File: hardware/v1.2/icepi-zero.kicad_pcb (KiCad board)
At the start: 4 copper layers, 65 x 30 mm, 160 parts, among them J1 Conn_02x20_Counter_Clockwise, J2 HDMI_C_1.3, J3 USB_C_Receptacle_USB2.0_14P, J4 USB_C_Receptacle_USB2.0_14P, J5 USB_C_Receptacle_USB2.0_14P, J6 Micro_SD_Card_Det2, SW1 SW_Push, SW2 SW_Push, U1 ECP5-CABGA256, U10 W9825G6KH, U11 W25Q128JVS, U2 TLV62569DBV, U3 TLV62569DBV, U4 TLV62569DBV, U5 PCA9306DC1, U6 FT231XQ, U7 TPD2EUSB30A, U8 TPD2EUSB30A, U9 TPD2EUSB30A, Y1 SITxxxxxx-1x-33E-50.000000

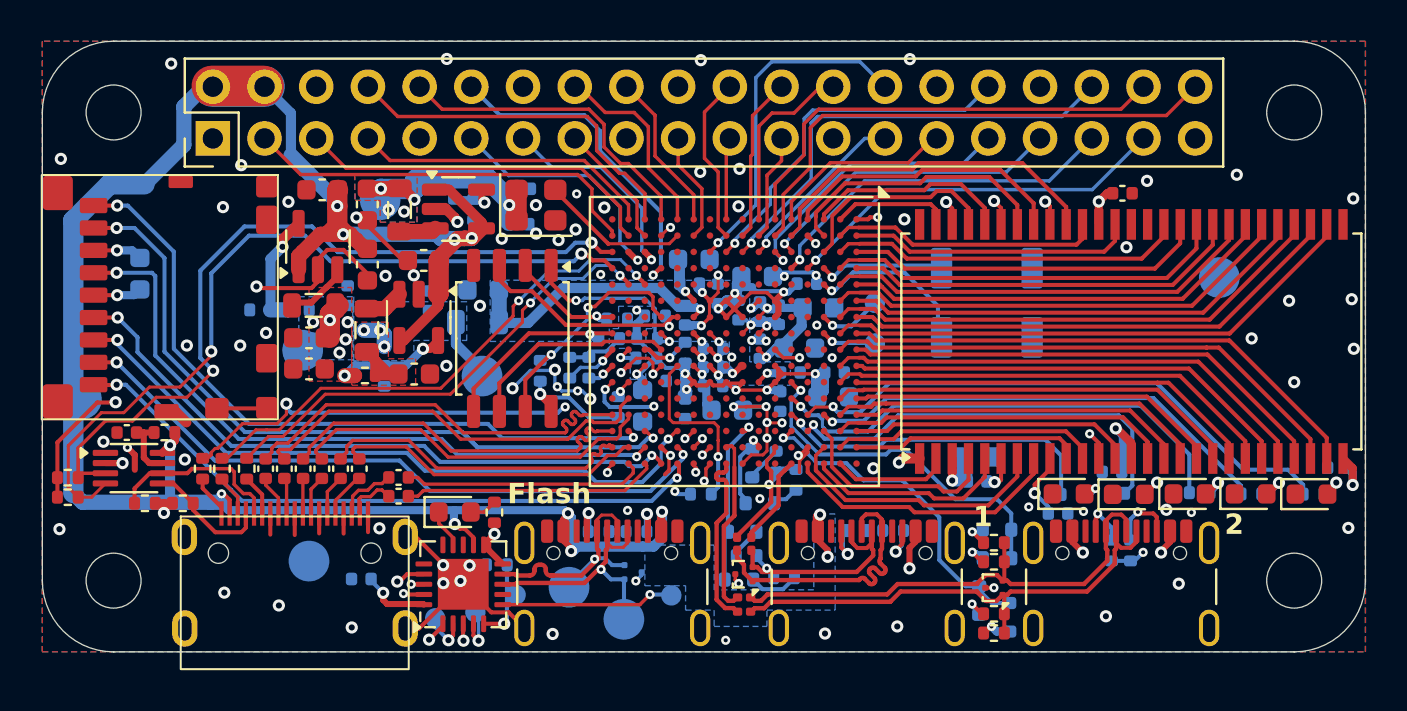
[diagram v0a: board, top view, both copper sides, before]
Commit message: UART to PS2 converter
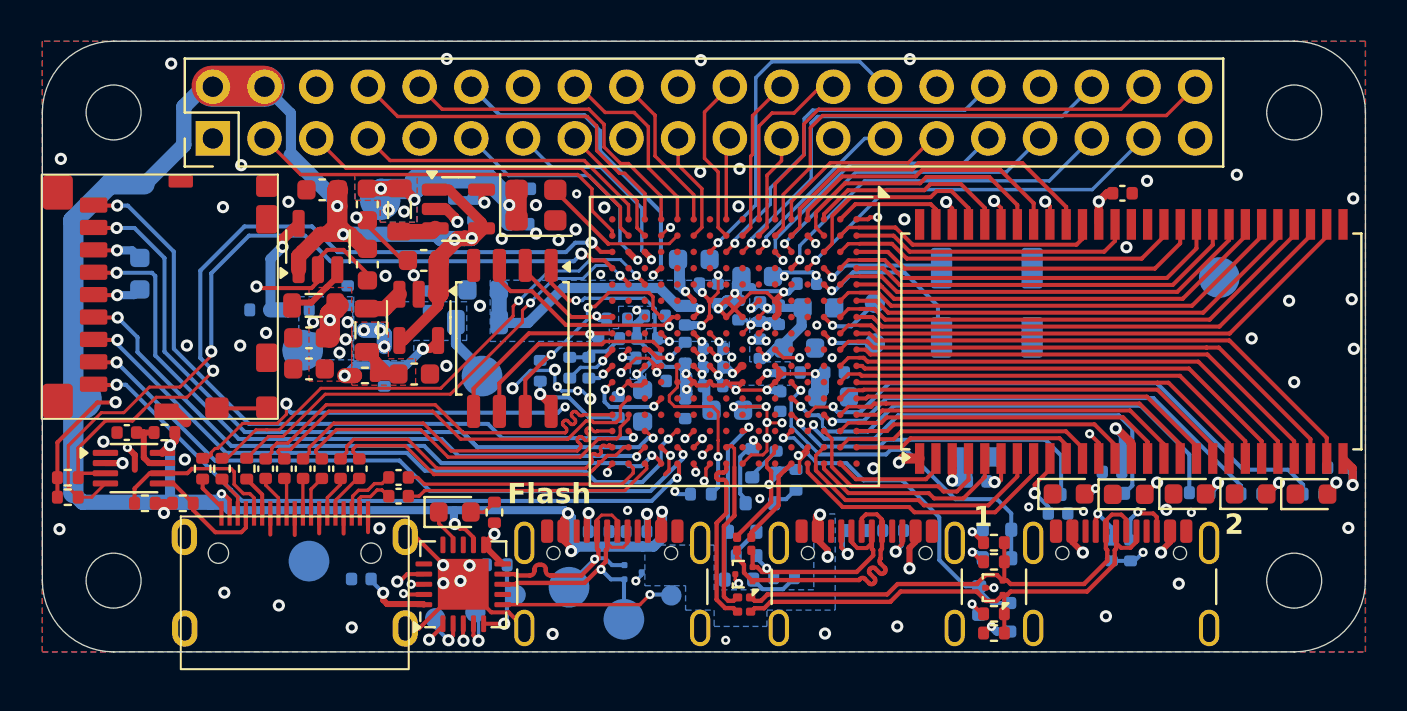
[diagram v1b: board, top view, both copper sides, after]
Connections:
- U1 pad M11: unconnected-(U1J-PR47A/+/HS/RSQ44-PadM11) -> JTAG_TDO
- U1 pad M9: unconnected-(U1J-PB18A/WRITEN-PadM9) -> (no net)
- U1 pad N12: unconnected-(U1J-PR44D/-/RSQ44-PadN12) -> JTAG_TMS
- U1 pad P11: unconnected-(U1J-PR47C/+/RSQ44/LRC_GPLL0T_IN-PadP11) -> JTAG_TDI
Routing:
- net JTAG_TDI: track 31.7 -> 32.6 mm
- net +3V3: track 95.4 -> 96.1 mm
- net JTAG_TMS: track 34.0 -> 34.5 mm

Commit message: Improve Makefile and v1.0 lpf
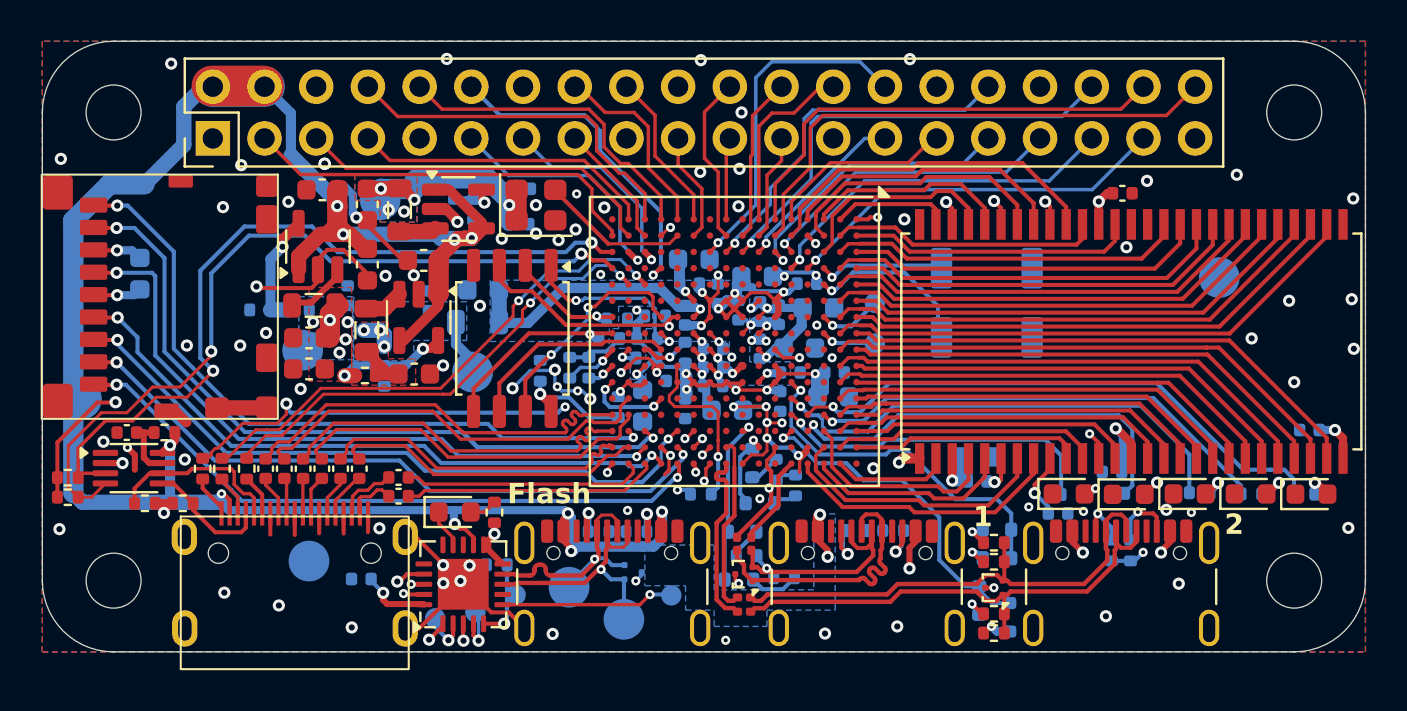
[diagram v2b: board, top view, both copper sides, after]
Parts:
- Y1: value SITxxxxxx-1x-33E-50.000000 -> SG-8018CG 50.000000MHz
- moved C39 2.31 mm to (178.2, 109.1)
- moved TP5 0.50 mm to (137.1, 106.2)
- moved R5 0.45 mm to (178.0, 112.2)
- moved R41 0.40 mm to (152.1, 111.0)
- moved R42 0.28 mm to (153.0, 111.8)
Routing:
- net GND: track 86.8 -> 90.6 mm, vias 110 -> 114
- net +5V: track 165.1 -> 167.0 mm
- net +1V1: track 39.0 -> 40.8 mm
- net Net-(D5-A): track 1.41 -> 0.86 mm
